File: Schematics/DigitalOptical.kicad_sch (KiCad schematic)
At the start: 118 parts, among them Q1 BSS138, Q2 BSS138, Q3 BSS138, Q4 BSS138, U49 LM1117-3.3, U50 PCF8575, U51 PC817, U52 PC817, U53 PC817, U54 PC817, U55 PC817, U56 PC817, U57 PC817, U58 PC817, U59 PC817, U60 PC817, U61 PC817, U62 PC817, U63 PC817, U64 PC817, U65 PC817, U66 PC817, U67 PC817, U68 PC817, U69 PC817, U70 PC817, U71 PC817, U72 PC817, U73 PC817, U74 PC817, U75 PC817, U76 PC817, U77 PC817, U78 PC817, U79 PC817, U80 PC817, U81 PC817, U82 PC817, U83 PCF8575, U84 LM1117-3.3

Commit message: Disp32 interface working properly.
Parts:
- renumbered R12 to R11, R13 to R12, R14 to R13, R15 to R14, R16 to R15, R17 to R16, R18 to R17, R19 to R18, R20 to R19, R21 to R20, R22 to R21, R23 to R22, R24 to R23, R25 to R24, R26 to R25, R27 to R26, R28 to R27, R29 to R28, R30 to R29, R31 to R30, R32 to R31, R33 to R32, R34 to R33, R35 to R34, R36 to R35, R37 to R36, R38 to R37, R39 to R38, R40 to R39, R41 to R40, R42 to R41, R43 to R42, R44 to R43, R45 to R44, R46 to R45, R47 to R46, R48 to R47, R49 to R48, R50 to R49, R51 to R50

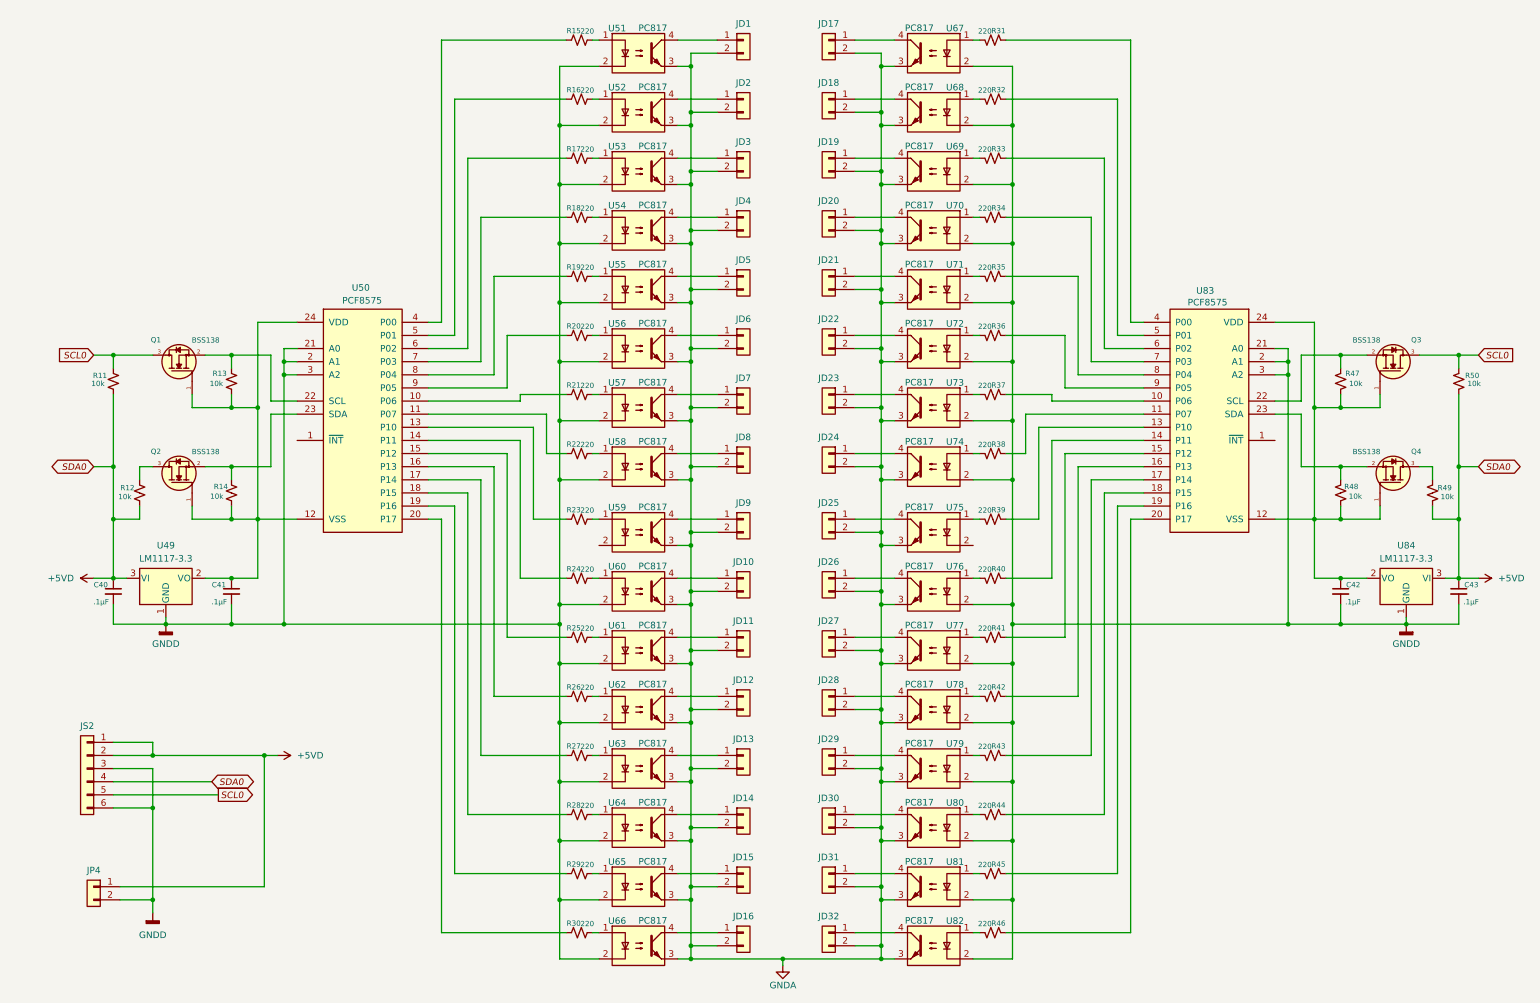
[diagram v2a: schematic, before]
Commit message: Noise generator and experimental steups.
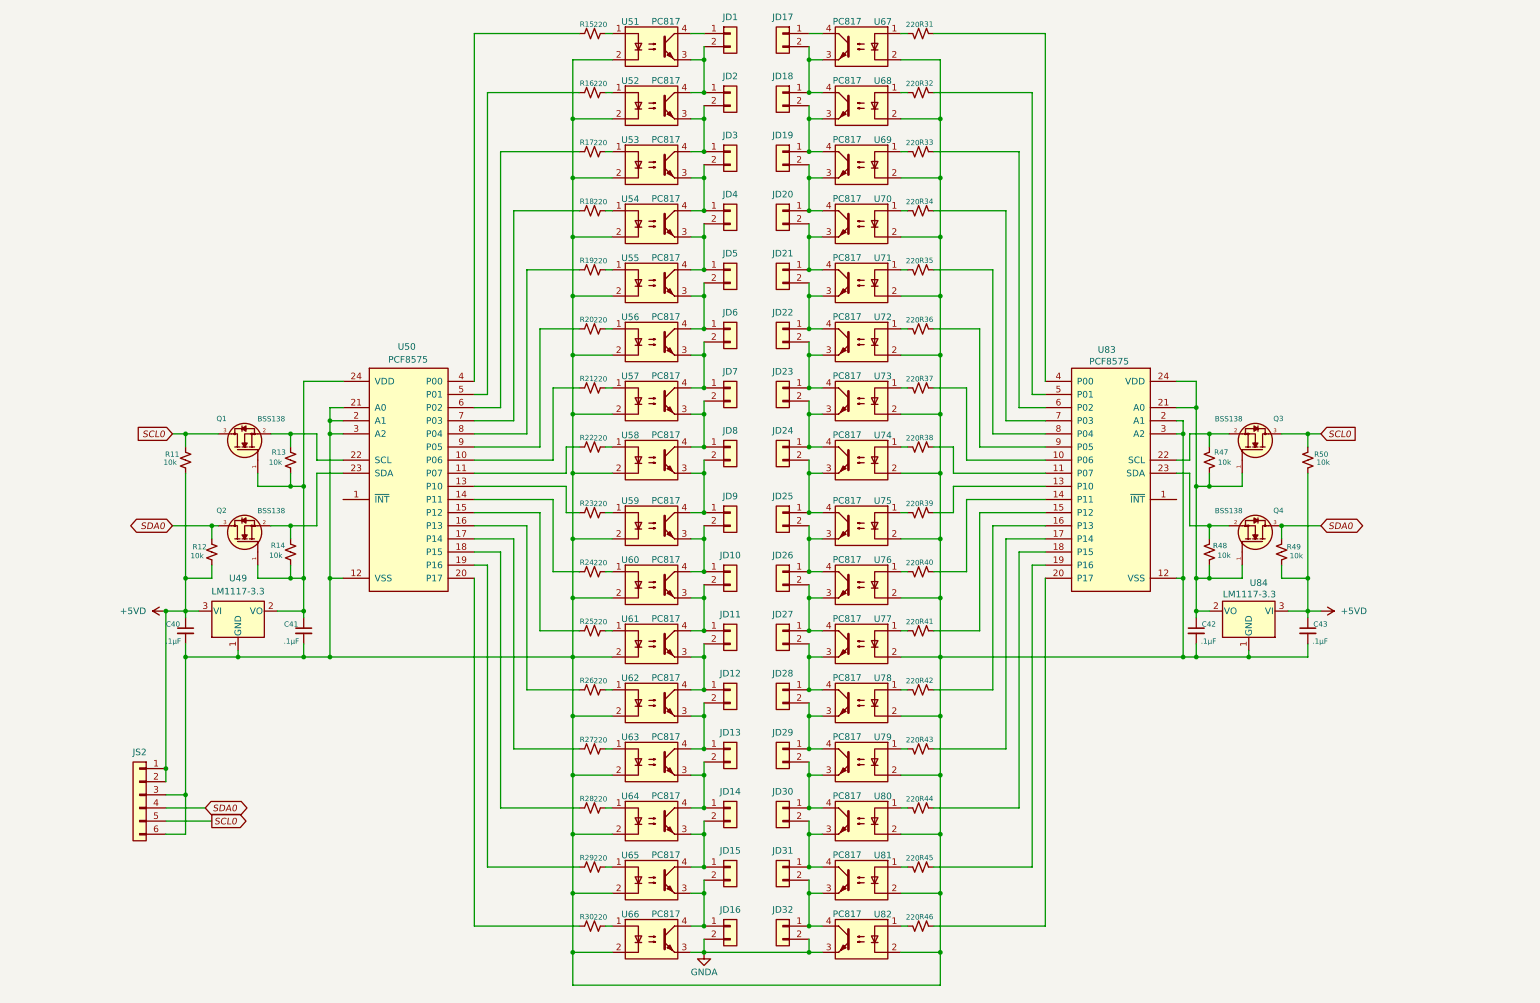
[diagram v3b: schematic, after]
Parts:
- removed JP4: From 12v Analog, symbol Connector_Generic:Conn_01x02
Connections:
- net +5VD: no longer JS2.4 (Pin_4)
- net GNDA: no longer JD1.2 (Pin_2), JD10.2 (Pin_2), JD11.2 (Pin_2), JD12.2 (Pin_2), JD13.2 (Pin_2), JD14.2 (Pin_2), JD15.2 (Pin_2), JD17.2 (Pin_2), JD18.2 (Pin_2), JD19.2 (Pin_2), JD2.2 (Pin_2), JD20.2 (Pin_2), JD21.2 (Pin_2), JD22.2 (Pin_2), JD23.2 (Pin_2), JD24.2 (Pin_2), JD25.2 (Pin_2), JD26.2 (Pin_2), JD27.2 (Pin_2), JD28.2 (Pin_2), JD29.2 (Pin_2), JD3.2 (Pin_2), JD30.2 (Pin_2), JD31.2 (Pin_2), JD4.2 (Pin_2), JD5.2 (Pin_2), JD6.2 (Pin_2), JD7.2 (Pin_2), JD8.2 (Pin_2), JD9.2 (Pin_2), U51.3, U52.3, U53.3, U54.3, U55.3, U56.3, U57.3, U58.3, U59.3, U60.3, U61.3, U62.3, U63.3, U64.3, U65.3, U67.3, U68.3, U69.3, U70.3, U71.3, U72.3, U73.3, U74.3, U75.3, U76.3, U77.3, U78.3, U79.3, U80.3, U81.3
- net at JD6.1 (Pin_1), U56.4: now also JD5.2 (Pin_2), U55.3
- net at JD26.1 (Pin_1), U76.4: now also JD25.2 (Pin_2), U75.3
- net at JD23.1 (Pin_1), U73.4: now also JD22.2 (Pin_2), U72.3
- net at JD31.1 (Pin_1), U81.4: now also JD30.2 (Pin_2), U80.3
- net at JD8.1 (Pin_1), U58.4: now also JD7.2 (Pin_2), U57.3
- net SDA0: now reaches Q2.3, R12.1
- net SDA0: now also JS2.4 (Pin_4), Q4.3, R49.1
- net at JD32.1 (Pin_1), U82.4: now also JD31.2 (Pin_2), U81.3
- net at C42.1, Q3.1, Q4.1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: now also U83.21 (A0); no longer U83.12 (VSS)
- net at JD22.1 (Pin_1), U72.4: now also JD21.2 (Pin_2), U71.3
- net at JD3.1 (Pin_1), U53.4: now also JD2.2 (Pin_2), U52.3
- net at JD10.1 (Pin_1), U60.4: now also JD9.2 (Pin_2), U59.3
- net at JD16.1 (Pin_1), U66.4: now also JD15.2 (Pin_2), U65.3
- net at JD27.1 (Pin_1), U77.4: now also JD26.2 (Pin_2), U76.3
- net at JD30.1 (Pin_1), U80.4: now also JD29.2 (Pin_2), U79.3
- net at JD13.1 (Pin_1), U63.4: now also JD12.2 (Pin_2), U62.3
- net at C41.1, Q1.1, Q2.1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: no longer U50.12 (VSS)
- net at JD4.1 (Pin_1), U54.4: now also JD3.2 (Pin_2), U53.3
- net at JD14.1 (Pin_1), U64.4: now also JD13.2 (Pin_2), U63.3
- net at JD5.1 (Pin_1), U55.4: now also JD4.2 (Pin_2), U54.3
- net at JD24.1 (Pin_1), U74.4: now also JD23.2 (Pin_2), U73.3
- net at JD11.1 (Pin_1), U61.4: now also JD10.2 (Pin_2), U60.3
- net at JD20.1 (Pin_1), U70.4: now also JD19.2 (Pin_2), U69.3
- net at JD25.1 (Pin_1), U75.4: now also JD24.2 (Pin_2), U74.3
- net at JD9.1 (Pin_1), U59.4: now also JD8.2 (Pin_2), U58.3
- net at JD7.1 (Pin_1), U57.4: now also JD6.2 (Pin_2), U56.3
- net at JD15.1 (Pin_1), U65.4: now also JD14.2 (Pin_2), U64.3
- net at JD12.1 (Pin_1), U62.4: now also JD11.2 (Pin_2), U61.3
- net at JD29.1 (Pin_1), U79.4: now also JD28.2 (Pin_2), U78.3
- net at U75.2: now also C40.2, C41.2, C42.2, C43.2, JS2.3 (Pin_3), JS2.6 (Pin_6), U49.1 (GND), U50.12 (VSS), U50.2 (A1), U50.21 (A0), U50.3 (A2), U51.2, U52.2, U53.2, U54.2, U55.2, U56.2, U57.2, U58.2, U59.2, U60.2, U61.2, U62.2, U63.2, U64.2, U65.2, U66.2, U67.2, U68.2, U69.2, U70.2, U71.2, U72.2, U73.2, U74.2, U76.2, U77.2, U78.2, U79.2, U80.2, U81.2, U82.2, U83.12 (VSS), U83.2 (A1), U83.3 (A2), U84.1 (GND)
- net at JD19.1 (Pin_1), U69.4: now also JD18.2 (Pin_2), U68.3
- net at JD2.1 (Pin_1), U52.4: now also JD1.2 (Pin_2), U51.3
- net at JD21.1 (Pin_1), U71.4: now also JD20.2 (Pin_2), U70.3
- net at JD28.1 (Pin_1), U78.4: now also JD27.2 (Pin_2), U77.3
- net at JD18.1 (Pin_1), U68.4: now also JD17.2 (Pin_2), U67.3
- removed net GNDD: C40.2, C41.2, C42.2, C43.2, JS2.3 (Pin_3), JS2.6 (Pin_6), U49.1 (GND), U50.2 (A1), U50.21 (A0), U50.3 (A2), U51.2, U52.2, U53.2, U54.2, U55.2, U56.2, U57.2, U58.2, U60.2, U61.2, U62.2, U63.2, U64.2, U65.2, U66.2, U67.2, U68.2, U69.2, U70.2, U71.2, U72.2, U73.2, U74.2, U76.2, U77.2, U78.2, U79.2, U80.2, U81.2, U82.2, U83.2 (A1), U83.21 (A0), U83.3 (A2), U84.1 (GND)
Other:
- moved on the sheet: C40, C41, C42, C43, JD1, JD10, JD11, JD12, JD13, JD14, JD15, JD16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

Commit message: adding noise source and variable state filter.
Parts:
- renumbered C40 to C36, C41 to C37, C42 to C38, C43 to C39, JS2 to JS3, U49 to U48, U50 to U49, U51 to U50, U52 to U51, U53 to U52, U54 to U53, U55 to U54, U56 to U55, U57 to U56, U58 to U57, U59 to U58, U60 to U59, U61 to U60, U62 to U61, U63 to U62, U64 to U63, U65 to U64, U66 to U65, U67 to U66, U68 to U67, U69 to U68, U70 to U69, U71 to U70, U72 to U71, U73 to U72, U74 to U73, U75 to U74, U76 to U75, U77 to U76, U78 to U77, U79 to U78, U80 to U79, U81 to U80, U82 to U81, U83 to U82, U84 to U83

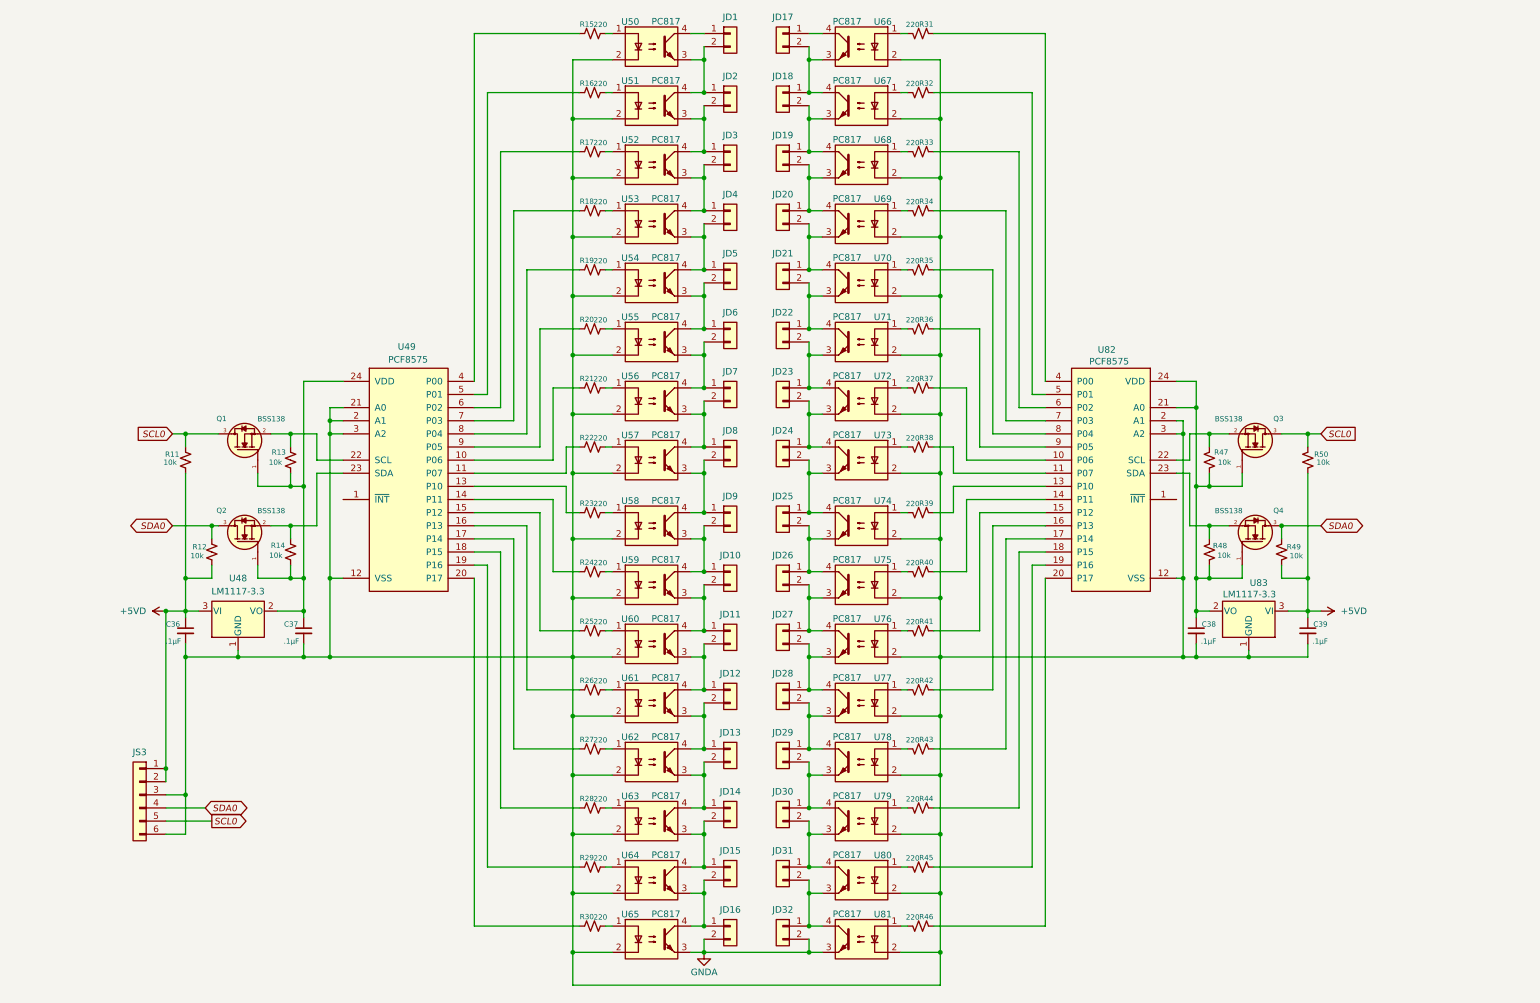
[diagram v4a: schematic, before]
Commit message: Noise boards added.
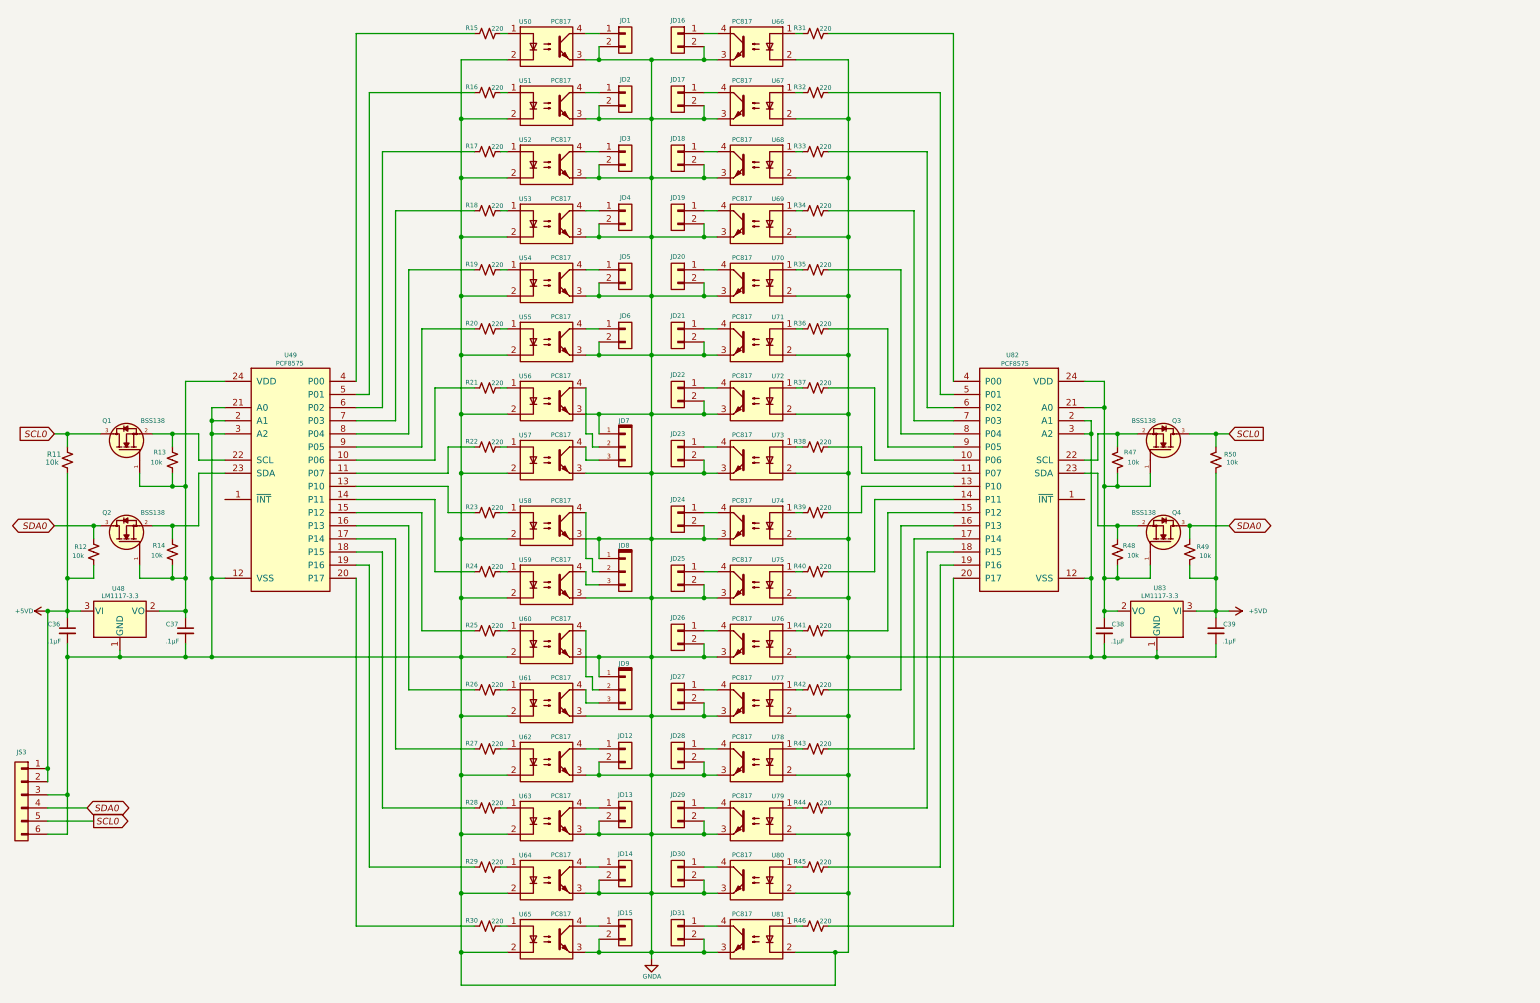
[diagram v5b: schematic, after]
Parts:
- removed JD10, JD11, JD16, JD32, JD7, JD8, JD9: From 12v Analog, symbol Connector_Generic:Conn_01x02
- added JD17: From 12v Analog, symbol Connector_Generic:Conn_01x02
- added JD7, JD8, JD9: Conn_01x03, symbol Connector_keyed_kicad_sym:Conn_01x03
- renumbered JD17 to JD16
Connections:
- net GNDA: now also JD1.2 (Pin_2), JD12.2 (Pin_2), JD13.2 (Pin_2), JD14.2 (Pin_2), JD15.2 (Pin_2), JD16.2 (Pin_2), JD18.2 (Pin_2), JD19.2 (Pin_2), JD2.2 (Pin_2), JD20.2 (Pin_2), JD21.2 (Pin_2), JD22.2 (Pin_2), JD23.2 (Pin_2), JD24.2 (Pin_2), JD25.2 (Pin_2), JD26.2 (Pin_2), JD27.2 (Pin_2), JD28.2 (Pin_2), JD29.2 (Pin_2), JD3.2 (Pin_2), JD30.2 (Pin_2), JD31.2 (Pin_2), JD4.2 (Pin_2), JD5.2 (Pin_2), JD6.2 (Pin_2), U50.3, U51.3, U52.3, U53.3, U54.3, U55.3, U56.3, U57.3, U58.3, U59.3, U60.3, U61.3, U62.3, U63.3, U64.3, U66.3, U67.3, U68.3, U69.3, U70.3, U71.3, U72.3, U73.3, U74.3, U75.3, U76.3, U77.3, U78.3, U79.3, U80.3, JD17.2 (Pin_2), JD7.1 (Pin_1), JD8.1 (Pin_1), JD9.1 (Pin_1)
- net at JD6.1 (Pin_1), U55.4: no longer JD5.2 (Pin_2), U54.3
- net at U66.1: now also R31.2; no longer R31.1
- net at R37.1: now also U82.10 (P06); no longer U72.1
- net at R37.2: now also U72.1; no longer U82.10 (P06)
- net at JD2.1 (Pin_1), U51.4: no longer JD1.2 (Pin_2), U50.3
- net at U58.4: now also JD8.2 (Pin_2); no longer U57.3
- net at U57.4: now also JD7.3 (Pin_3); no longer U56.3
- net at U81.1: now also R46.2; no longer R46.1
- net at R36.1: now also U82.9 (P05); no longer U71.1
- net at JD4.1 (Pin_1), U53.4: no longer JD3.2 (Pin_2), U52.3
- net at JD3.1 (Pin_1), U52.4: no longer JD2.2 (Pin_2), U51.3
- net at R45.1: now also U82.19 (P16); no longer U80.1
- net at R45.2: now also U80.1; no longer U82.19 (P16)
- net at U60.4: now also JD9.2 (Pin_2); no longer U59.3
- net at U59.4: now also JD8.3 (Pin_3); no longer U58.3
- net at U79.1: now also R44.2; no longer R44.1
- net at U82.18 (P15): now also R44.1; no longer R44.2
- net at U76.1: now also R41.2; no longer R41.1
- net at U75.1: now also R40.2; no longer R40.1
- net at JD5.1 (Pin_1), U54.4: no longer JD4.2 (Pin_2), U53.3
- net at R36.2: now also U71.1; no longer U82.9 (P05)
- net at U82.20 (P17): now also R46.1; no longer R46.2
- net at R39.1: now also U82.13 (P10); no longer U74.1
- net at R39.2: now also U74.1; no longer U82.13 (P10)
- net at R38.1: now also U82.11 (P07); no longer U73.1
- net at U69.1: now also R34.2; no longer R34.1
- net at U82.7 (P03): now also R34.1; no longer R34.2
- net at R42.1: now also U82.16 (P13); no longer U77.1
- net at R42.2: now also U77.1; no longer U82.16 (P13)
- net at R33.1: now also U82.6 (P02); no longer U68.1
- net at R38.2: now also U73.1; no longer U82.11 (P07)
- net at U82.14 (P11): now also R40.1; no longer R40.2
- net at U82.15 (P12): now also R41.1; no longer R41.2
- net at U82.17 (P14): now also R43.1; no longer R43.2
- net at U82.4 (P00): now also R31.1; no longer R31.2
- net at U82.5 (P01): now also R32.1; no longer R32.2
- net at R33.2: now also U68.1; no longer U82.6 (P02)
- net at U82.8 (P04): now also R35.1; no longer R35.2
- net at U70.1: now also R35.2; no longer R35.1
- net at U67.1: now also R32.2; no longer R32.1
- net at U78.1: now also R43.2; no longer R43.1
- new net: JD15.1 (Pin_1), U65.4
- new net: JD29.1 (Pin_1), U79.4
- new net: JD19.1 (Pin_1), U69.4
- new net: JD7.2 (Pin_2), U56.4
- new net: JD14.1 (Pin_1), U64.4
- new net: JD26.1 (Pin_1), U76.4
- new net: JD25.1 (Pin_1), U75.4
- new net: JD22.1 (Pin_1), U72.4
- new net: JD31.1 (Pin_1), U81.4
- new net: JD28.1 (Pin_1), U78.4
- new net: JD30.1 (Pin_1), U80.4
- new net: JD21.1 (Pin_1), U71.4
- new net: JD23.1 (Pin_1), U73.4
- new net: JD13.1 (Pin_1), U63.4
- new net: JD20.1 (Pin_1), U70.4
- new net: JD12.1 (Pin_1), U62.4
- new net: JD18.1 (Pin_1), U68.4
- new net: JD9.3 (Pin_3), U61.4
- new net: JD17.1 (Pin_1), U67.4
- new net: JD27.1 (Pin_1), U77.4
- new net: JD24.1 (Pin_1), U74.4
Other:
- moved on the sheet: C36, C37, C38, C39, JD1, JD16, JS3, Q1, Q3, R11, R12, R13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
